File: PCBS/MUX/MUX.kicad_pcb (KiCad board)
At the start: 2 copper layers, 29 x 14 mm, 17 parts, among them J1 Conn_01x01_Socket, J2 Conn_01x01_Socket, J3 Conn_01x03_Socket, J6 Conn_01x01_Socket, U1 SN74LVC2G157DCTR

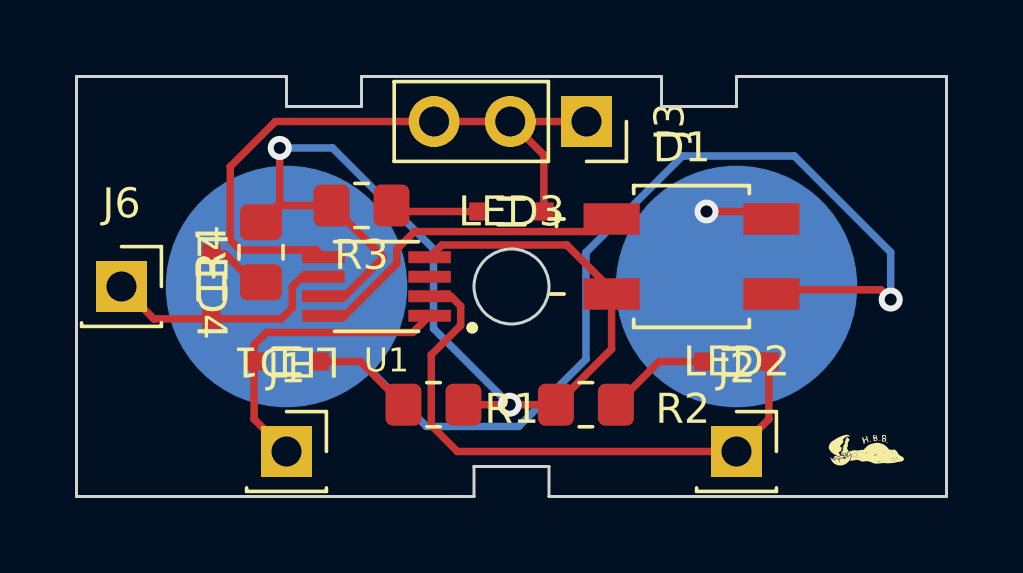
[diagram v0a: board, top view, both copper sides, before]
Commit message: Fixed mux
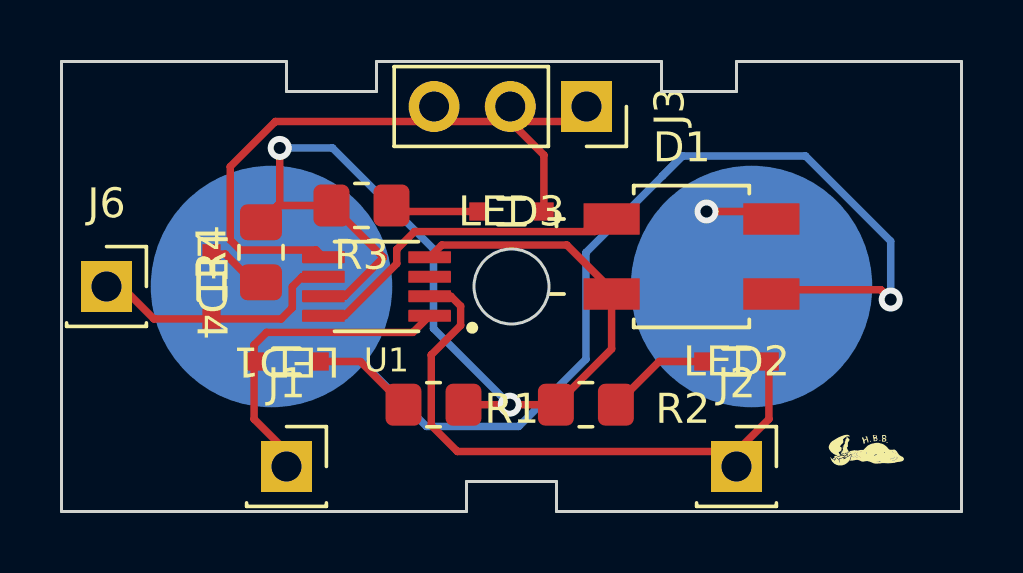
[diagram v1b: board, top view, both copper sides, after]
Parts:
- moved J1 0.50 mm to (147.5, 93.5)
- moved J2 0.50 mm to (162.5, 93.5)
- moved J3 0.50 mm to (157.5, 81.5)
- moved J4 0.50 mm to (147.0, 87.5)
- moved J5 0.50 mm to (163.0, 87.5)
- moved J6 0.50 mm to (141.5, 87.5)
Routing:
- net Net-(J4-PWR): track 34.9 -> 36.1 mm
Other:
- board size 29 x 14 mm -> 30 x 15 mm
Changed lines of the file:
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@@
   )
   (footprint "Connector_PinSocket_2.54mm:PinSocket_1x01_P2.54mm_Vertical" locked (layer "F.Cu")
-    (at 147.5 93)
+    (at 147.5 93.5)
     (descr "Through hole straight socket strip, 1x01, 2.54mm pitch, single row (from Kicad 4.0.7), script generated")
     (tags "Through hole socket strip THT 1x01 2.54mm single row")
@@
   )
   (footprint "Connector_PinSocket_2.54mm:PinSocket_1x01_P2.54mm_Vertical" locked (layer "F.Cu")
-    (at 162.5 93)
+    (at 162.5 93.5)
     (descr "Through hole straight socket strip, 1x01, 2.54mm pitch, single row (from Kicad 4.0.7), script generated")
     (tags "Through hole socket strip THT 1x01 2.54mm single row")
@@
   )
   (footprint "Connector_PinSocket_2.54mm:PinSocket_1x03_P2.54mm_Vertical" locked (layer "F.Cu")
-    (at 157.5 82 -90)
+    (at 157.5 81.5 -90)
     (descr "Through hole straight socket strip, 1x03, 2.54mm pitch, single row (from Kicad 4.0.7), script generated")
     (tags "Through hole socket strip THT 1x03 2.54mm single row")
@@
   )
   (footprint "Connector_PinSocket_2.54mm:PinSocket_1x01_P2.54mm_Vertical" locked (layer "F.Cu")
-    (at 142 87.5)
+    (at 141.5 87.5)
     (descr "Through hole straight socket strip, 1x01, 2.54mm pitch, single row (from Kicad 4.0.7), script generated")
     (tags "Through hole socket strip THT 1x01 2.54mm single row")
@@
   )
   (footprint "DigitalLogicFootprints:8mm-snap" locked (layer "B.Cu")
-    (at 147.5 87.5 180)
+    (at 147 87.5 180)
     (property "Sheetfile" "MUX.kicad_sch")
     (property "Sheetname" "")
@@
   )
   (footprint "DigitalLogicFootprints:8mm-snap" locked (layer "B.Cu")
-    (at 162.5 87.5 180)
+    (at 163 87.5 180)
     (property "Sheetfile" "MUX.kicad_sch")
     (property "Sheetname" "")
@@
       (net 9 "Net-(J5-PWR)") (pinfunction "PWR") (pintype "output"))
   )
-  (gr_poly
-    (pts
-      (xy 169.5 80.5)
-      (xy 162.5 80.5)
-      (xy 162.5 81.5)
-      (xy 160 81.5)
-      (xy 160 80.5)
-      (xy 150 80.5)
-      (xy 150 81.5)
-      (xy 147.5 81.5)
-      (xy 147.5 80.5)
-      (xy 140.5 80.5)
-      (xy 140.5 94.5)
-      (xy 153.75 94.5)
-      (xy 153.75 93.5)
-      (xy 156.25 93.5)
-      (xy 156.25 94.5)
-      (xy 169.5 94.5)
-    )
-    (stroke (width 0.1) (type solid)) (fill none) (layer "Edge.Cuts"))
   (gr_circle (center 165.1 81.28) (end 165.1 81.28)
     (stroke (width 0.1) (type default)) (fill none) (layer "Edge.Cuts"))
   (gr_circle (center 155 87.5) (end 156.25 87.5)
     (stroke (width 0.1) (type default)) (fill none) (layer "Edge.Cuts"))
+  (gr_poly
+    (pts
+      (xy 140 80)
+      (xy 147.5 80)
+      (xy 147.5 81)
+      (xy 150.5 81)
+      (xy 150.5 80)
+      (xy 160 80)
+      (xy 160 81)
+      (xy 162.5 81)
+      (xy 162.5 80)
+      (xy 170 80)
+      (xy 170 95)
+      (xy 156.5 95)
+      (xy 156.5 94)
+      (xy 153.5 94)
+      (xy 153.5 95)
+      (xy 140 95)
+    )
+    (stroke (width 0.1) (type solid)) (fill none) (layer "Edge.Cuts"))
   (segment (start 149 84.8) (end 147.21 84.8) (width 0.25) (layer "F.Cu") (net 1))
   (segment (start 147.21 84.8) (end 146.65 85.36) (width 0.25) (layer "F.Cu") (net 1))
@@
   (via (at 167.64 87.935641) (size 0.8) (drill 0.4) (layers "F.Cu" "B.Cu") (free) (net 10))
   (segment (start 147.5 87.5) (end 152.165 92.165) (width 0.25) (layer "B.Cu") (net 10))
-  (segment (start 164.43 83.15) (end 167.64 86.36) (width 0.25) (layer "B.Cu") (net 10))
+  (segment (start 160.698172 83.15) (end 160.024086 83.824086) (width 0.25) (layer "B.Cu") (net 10))
+  (segment (start 164.801829 83.15) (end 160.698172 83.15) (width 0.25) (layer "B.Cu") (net 10))
   (segment (start 157.48 89.925305) (end 157.48 86.368171) (width 0.25) (layer "B.Cu") (net 10))
-  (segment (start 160.698171 83.15) (end 164.43 83.15) (width 0.25) (layer "B.Cu") (net 10))
-  (segment (start 167.64 86.36) (end 167.64 87.935641) (width 0.25) (layer "B.Cu") (net 10))
+  (segment (start 160.024086 83.824086) (end 160.698171 83.15) (width 0.25) (layer "B.Cu") (net 10))
   (segment (start 152.165 92.165) (end 155.240305 92.165) (width 0.25) (layer "B.Cu") (net 10))
-  (segment (start 157.48 86.368171) (end 160.698171 83.15) (width 0.25) (layer "B.Cu") (net 10))
+  (segment (start 167.64 85.988171) (end 164.801829 83.15) (width 0.25) (layer "B.Cu") (net 10))
+  (segment (start 157.48 86.368171) (end 160.024086 83.824086) (width 0.25) (layer "B.Cu") (net 10))
+  (segment (start 167.64 87.935641) (end 167.64 85.988171) (width 0.25) (layer "B.Cu") (net 10))
   (segment (start 155.240305 92.165) (end 157.48 89.925305) (width 0.25) (layer "B.Cu") (net 10))
   (segment (start 148.022096 87.175) (end 148.73 87.175) (width 0.25) (layer "F.Cu") (net 11))
